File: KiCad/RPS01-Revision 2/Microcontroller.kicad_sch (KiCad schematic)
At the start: 13 parts

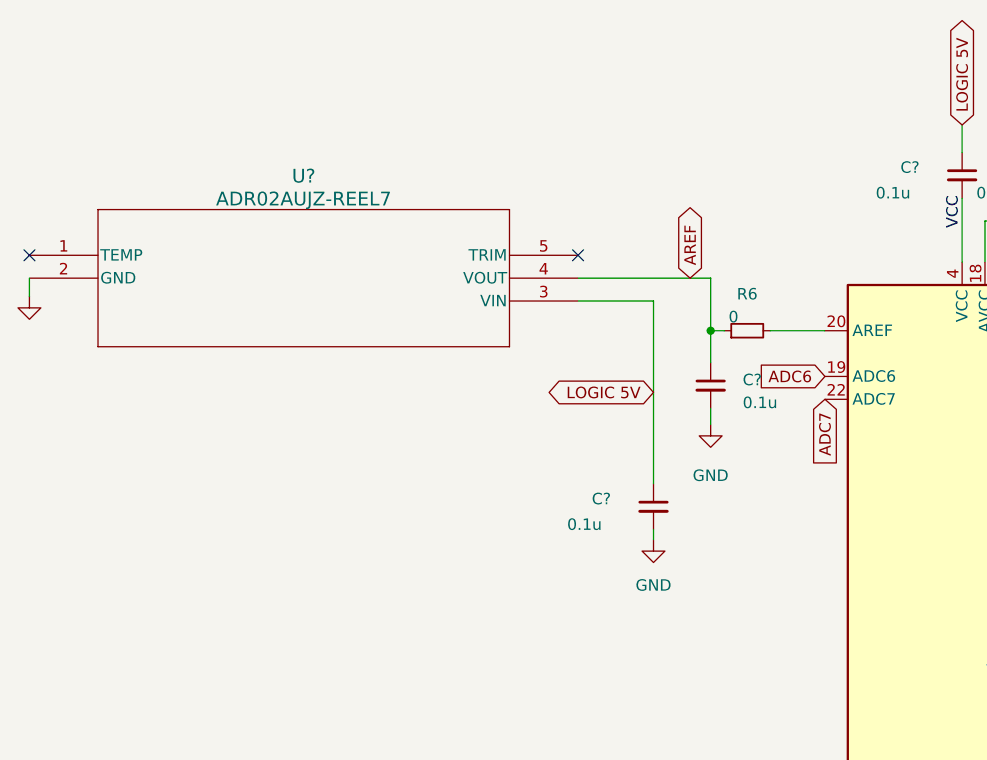
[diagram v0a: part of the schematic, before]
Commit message: Updated Buffer, Precision LDO, new LDO
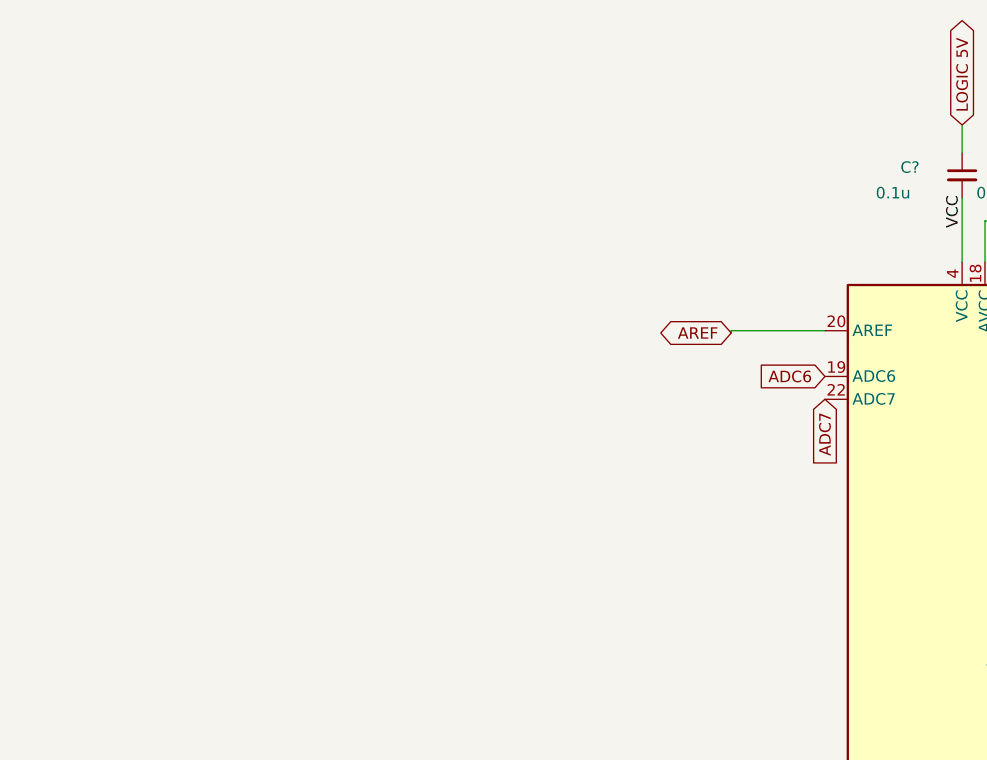
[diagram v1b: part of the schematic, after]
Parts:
- removed C? (x2): 0.1u, Capacitor_SMD:C_0603_1608Metric, symbol Device:C_Small
- removed R6: 0, Resistor_SMD:R_0603_1608Metric, symbol Device:R_Small
- removed U?: ADR02AUJZ-REEL7, Mechatronics VREF:UJ_5_ADI, symbol 2023-06-26_00-14-37:ADR02AUJZ-REEL7
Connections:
- net AREF: now also U?.20 (AREF)
- no-connect marks 2 -> 0

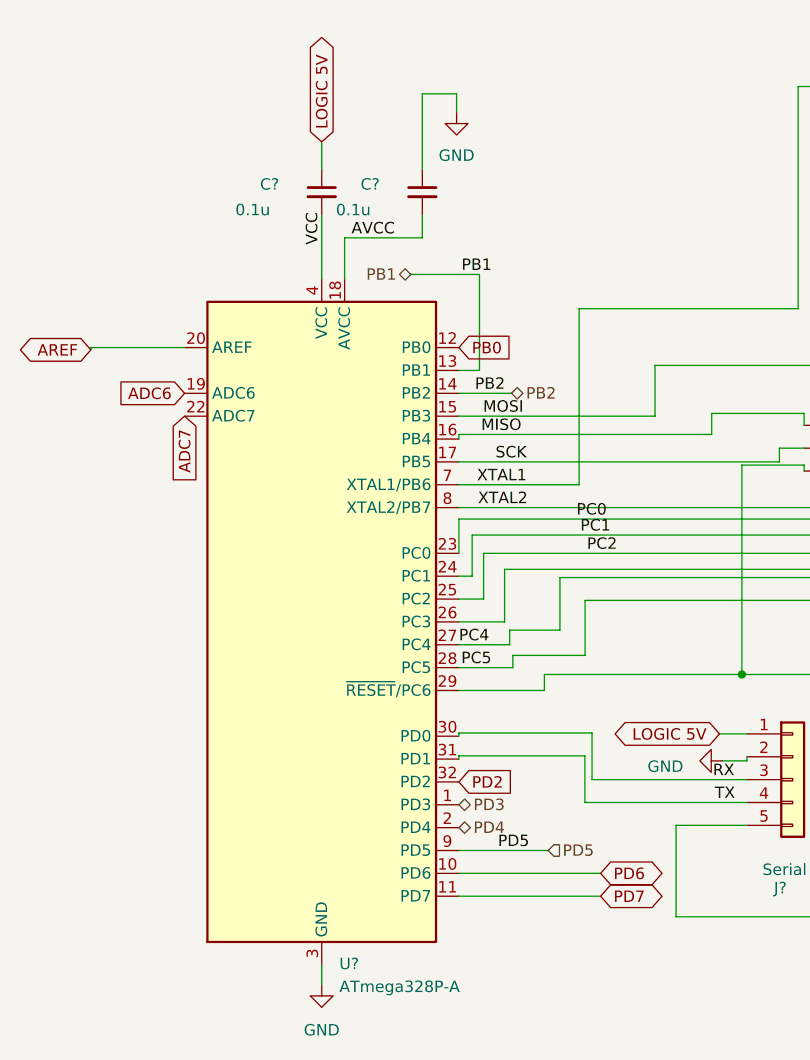
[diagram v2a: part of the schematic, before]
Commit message: Update Microcontroller.kicad_sch
Added pull-down resistors and fixed AVCC and VCC connections with filter cap.
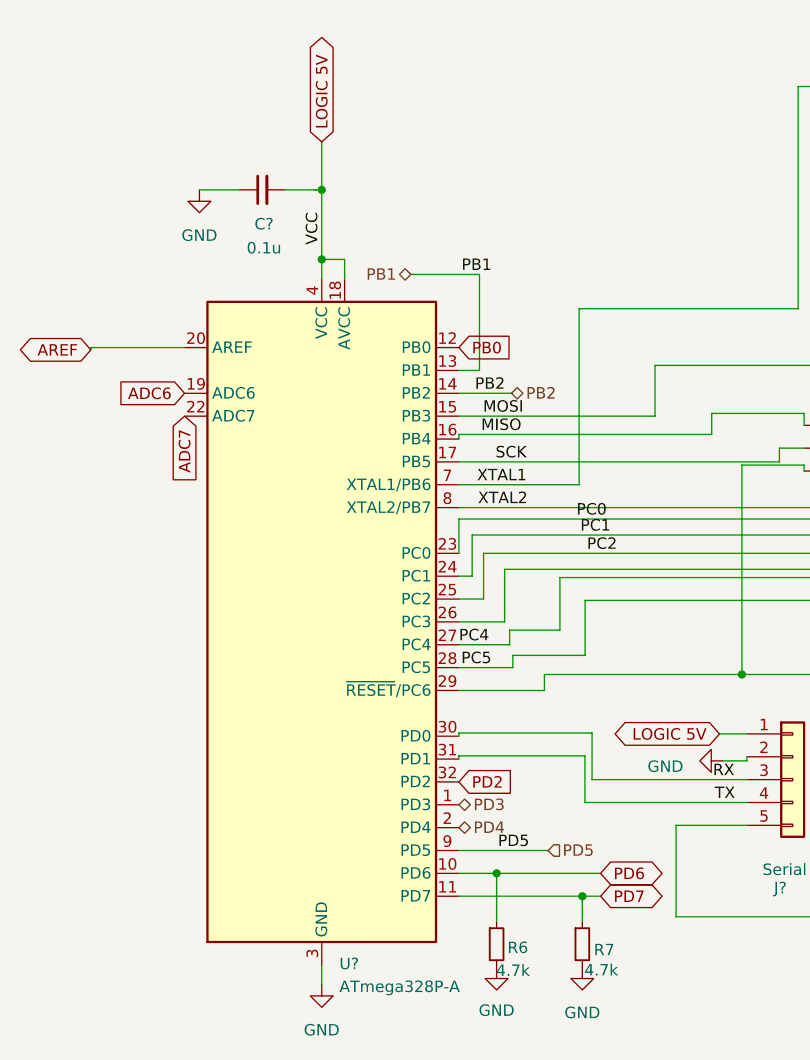
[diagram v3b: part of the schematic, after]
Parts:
- removed C?: 0.1u, Capacitor_SMD:C_0603_1608Metric, symbol Device:C_Small
- added R6, R7: 4.7k, Resistor_SMD:R_0603_1608Metric, symbol Device:R_Small
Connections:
- net AVCC is gone; now on net LOGIC 5V: U?.18 (AVCC)
- net VCC is gone; now on net LOGIC 5V: C?.2, U?.4 (VCC), U?.6 (VCC)
- net GND: now also C?.1, R6.2, R7.2
- net LOGIC 5V: no longer C?.1
- net PD6: now also R6.1
- net PD7: now also R7.1
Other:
- moved on the sheet: C?

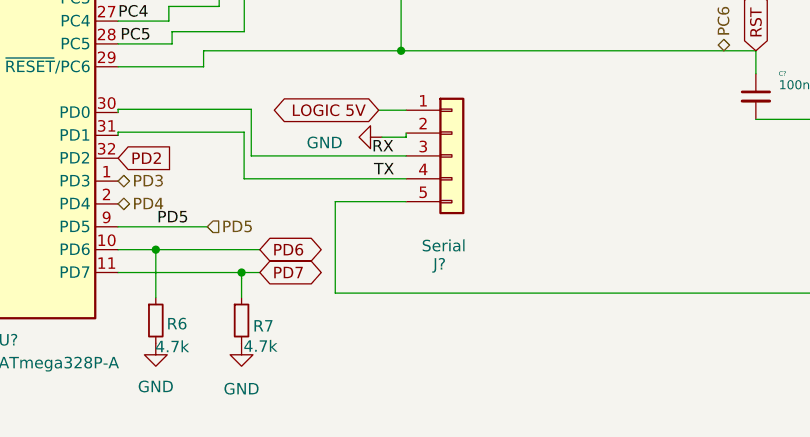
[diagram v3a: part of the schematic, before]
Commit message: Only Switches left
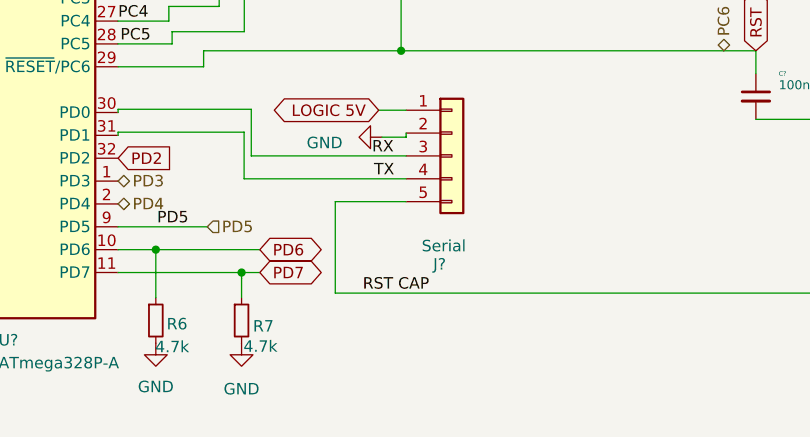
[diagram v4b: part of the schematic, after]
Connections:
- net RST CAP: now reaches C?.2, J?.5 (Pin_5)
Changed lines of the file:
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@@
+    (effects (font (size 1.27 1.27)) (justify left bottom))
+  )
+  (label "RST CAP" (at 162.052 169.672 0) (fields_autoplaced)
     (effects (font (size 1.27 1.27)) (justify left bottom))
   )
